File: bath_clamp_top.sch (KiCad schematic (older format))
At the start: 80 parts, among them J1 105-1103-001, J2 105-1103-001, J3 105-1103-001, J4 HDMI_A, K1 1462042-7, K2 1462042-7, Q1 MBT3904DW1T1G, Q3 MBT3904DW1T1G, Q4 MBT3904DW1T1G, U1 OPA828, U12 TCA9555DBR, U13 TCA9555DBR, U19 TMUX6136PWR, U2 ADG1208, U25 OPA2156xD, U3 G6L-1F-TR-DC5, U4 G6L-1F-TR-DC5, U5 G6L-1F-TR-DC5, U8 OPA2156xD

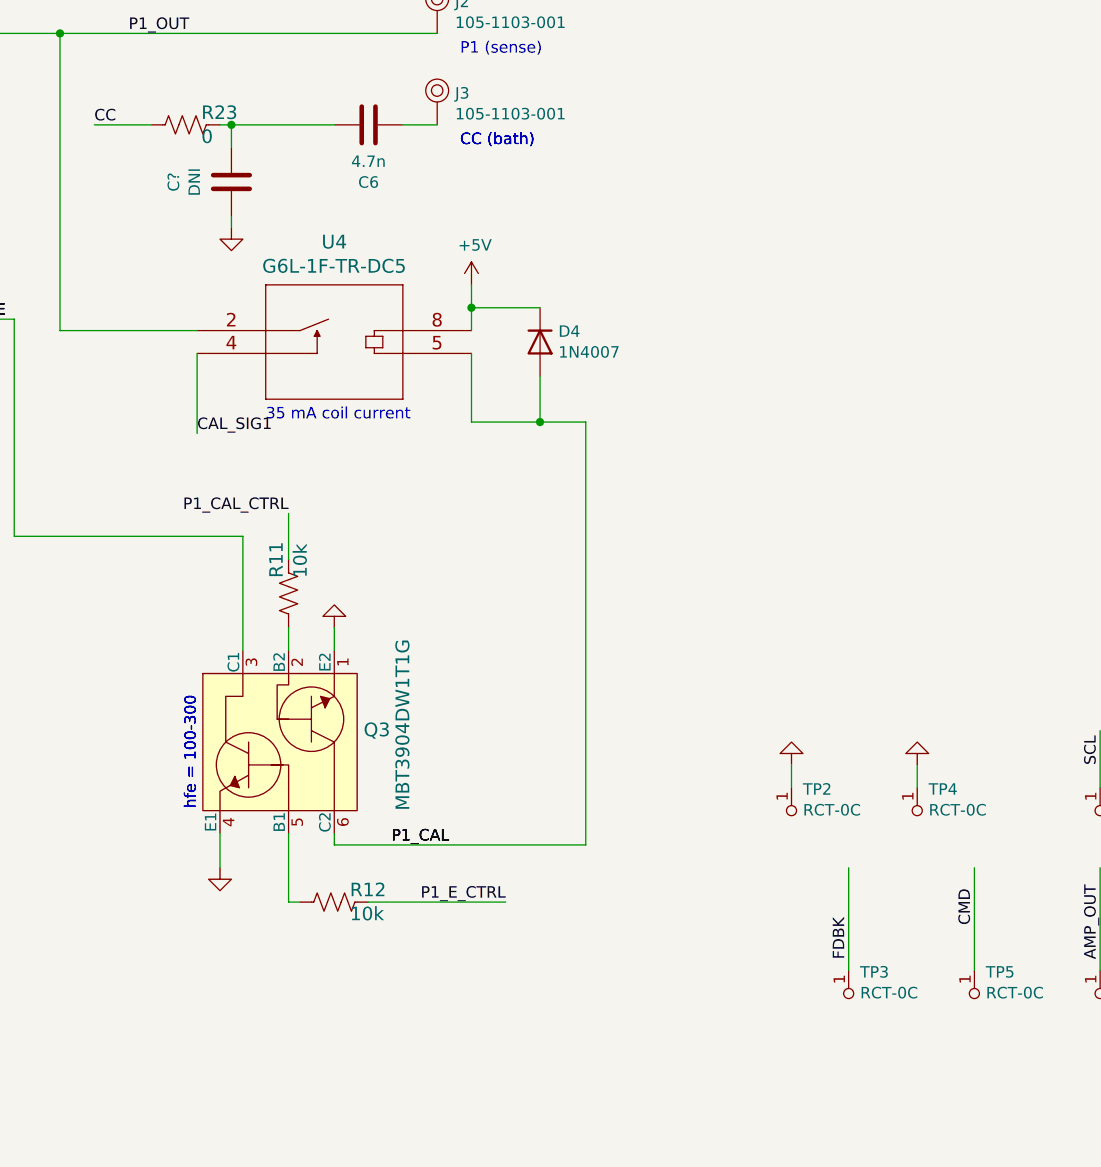
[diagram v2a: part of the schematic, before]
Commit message: nearly completed layout re-route
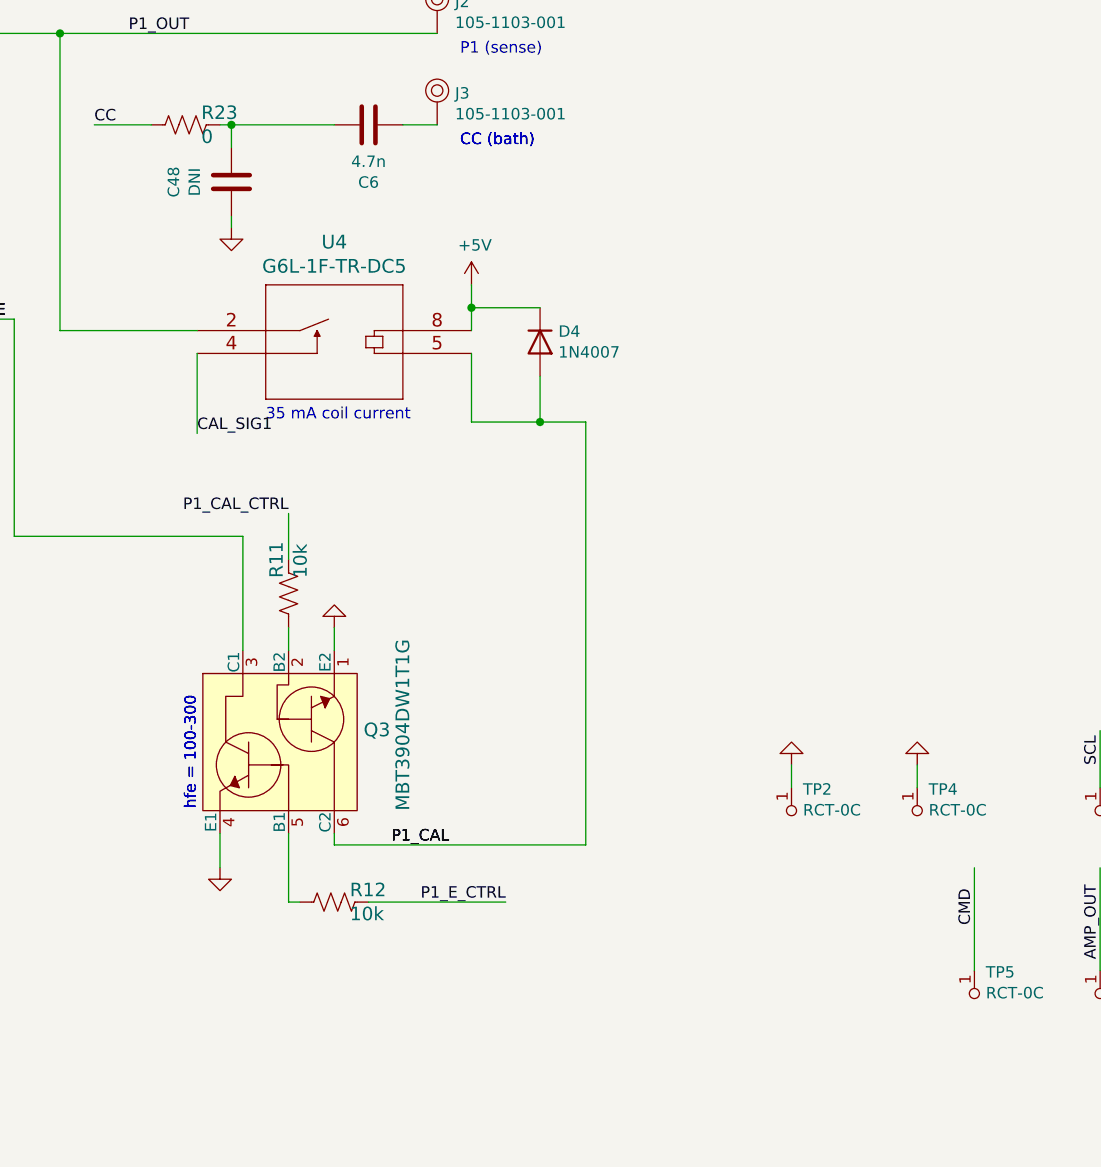
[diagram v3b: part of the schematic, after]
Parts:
- removed TP3: RCT-0C, digikey-footprints:PROBE_PAD_0805, symbol dk_Test-Points:RCT-0C
- gave numbers to parts that had none: 1
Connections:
- wire segments 373 -> 372
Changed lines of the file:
@@
-$EndComp
-$Comp
-L dk_Test-Points:RCT-0C TP3
-U 1 1 6153F62F
-P 14350 9000
-F 0 "TP3" H 14400 9093 50  0000 L CNN
-F 1 "RCT-0C" H 14400 9002 50  0000 L CNN
-F 2 "digikey-footprints:PROBE_PAD_0805" H 14550 9200 60  0001 L CNN
-F 3 "https://www.te.com/commerce/DocumentDelivery/DDEController?Action=srchrtrv&DocNm=1773266&DocType=DS&DocLang=English" H 14550 9300 60  0001 L CNN
-F 4 "A106144CT-ND" H 14550 9400 60  0001 L CNN "Digi-Key_PN"
-F 5 "RCT-0C" H 14550 9500 60  0001 L CNN "MPN"
-F 6 "Test and Measurement" H 14550 9600 60  0001 L CNN "Category"
-F 7 "Test Points" H 14550 9700 60  0001 L CNN "Family"
-F 8 "https://www.te.com/commerce/DocumentDelivery/DDEController?Action=srchrtrv&DocNm=1773266&DocType=DS&DocLang=English" H 14550 9800 60  0001 L CNN "DK_Datasheet_Link"
-F 9 "/product-detail/en/te-connectivity-amp-connectors/RCT-0C/A106144CT-ND/3477801" H 14550 9900 60  0001 L CNN "DK_Detail_Page"
-F 10 "PC TEST POINT NATURAL" H 14550 10000 60  0001 L CNN "Description"
-F 11 "TE Connectivity AMP Connectors" H 14550 10100 60  0001 L CNN "Manufacturer"
-F 12 "Active" H 14550 10200 60  0001 L CNN "Status"
-F 13 "RCT-0C" H 14350 9000 50  0001 C CNN "Manf#"
-	1    14350 9000
-	1    0    0    -1
 $EndComp
 $Comp
@@
 CMD
 Wire Wire Line
-	14350 8900 14350 8450
-Wire Wire Line
 	15450 8100 15450 7850
 Wire Wire Line
@@
 Wire Wire Line
 	14650 8100 14650 8000
-Text Label 14350 8850 1    50   ~ 0
-FDBK
 $Comp
 L dk_Test-Points:RCT-0C TP1
@@
 6.0 mm by \n10.0 mm
 $Comp
-L Device:C C?
+L Device:C C48
 U 1 1 62573817
 P 11650 5450
-F 0 "C?" V 11398 5450 50  0000 C CNN
+F 0 "C48" V 11398 5450 50  0000 C CNN
 F 1 "DNI" V 11489 5450 50  0000 C CNN
 F 2 "Capacitor_SMD:C_0603_1608Metric" H 11688 5300 50  0001 C CNN
@@
 $EndComp
 $Comp
-L power:GND #PWR?
+L power:GND #PWR0188
 U 1 1 625748EF
 P 11650 5650
-F 0 "#PWR?" H 11650 5400 50  0001 C CNN
+F 0 "#PWR0188" H 11650 5400 50  0001 C CNN
 F 1 "GND" V 11655 5522 50  0001 R CNN
 F 2 "" H 11650 5650 50  0001 C CNN
@@
 Wire Wire Line
 	11650 5300 11650 5200
+Connection ~ 11650 5200
+Wire Wire Line
+	11650 5200 12100 5200
 Wire Bus Line
 	9200 9450 9200 9750
@@
 Wire Bus Line
 	3500 8000 3500 8450
-Connection ~ 11650 5200
-Wire Wire Line
-	11650 5200 12100 5200
 $EndSCHEMATC

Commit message: gerbers, BOM and fabrication files sent to PCBway
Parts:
- added C49: DNI, Capacitor_SMD:C_0603_1608Metric, symbol Device:C
- added J5: Conn_01x04, Connector_PinHeader_2.54mm:PinHeader_1x04_P2.54mm_Vertical, symbol Connector_Generic:Conn_01x04
- added TP13, TP14, TP15: TestPoint, TestPoint:TestPoint_THTPad_D2.0mm_Drill1.0mm, symbol Connector:TestPoint
- J1: Category Connectors, Interconnects -> (none); DK_Datasheet_Link https://belfuse.com/resources/Johnson/drawings/dr-105110100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 -> (none); DK_Detail_Page /product-detail/en/cinch-connectivity-solutions-johnson/105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 -> (none); Digi-Key_PN J577-ND -> (none); Family Banana and Tip Connectors - Jacks, Plugs -> (none); MPN 105-1103-001 -> (none); Manufacturer (none) -> Cinch Connectivity Solutions Johnson; Status Active -> (none)
- J2, J3: Category Connectors, Interconnects -> (none); DK_Datasheet_Link https://belfuse.com/resources/Johnson/drawings/dr-105110100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 -> (none); DK_Detail_Page /product-detail/en/cinch-connectivity-solutions-johnson/105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 -> (none); Digi-Key_PN J577-ND -> (none); Family Banana and Tip Connectors - Jacks, Plugs -> (none); MPN 105-1103-001 -> (none); Status Active -> (none)
- K1, K2: footprint covg-kicad:Relay_SPDT_TE_1462042-7 -> RELAY_1462042-8
- Q1: footprint Package_TO_SOT_SMD:SOT-363_SC-70-6 -> digikey-footprints:SOT-363; Category Discrete Semiconductor Products -> (none); DK_Datasheet_Link http://www.onsemi.com/pub/Collateral/MBT3904DW1T1-D.PDF -> (none); DK_Detail_Page /product-detail/en/on-semiconductor/MBT3904DW1T1G/MBT3904DW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 -> (none); Digi-Key_PN MBT3904DW1T1GOSCT-ND -> (none); Family Transistors - Bipolar (BJT) - Arrays -> (none); MPN MBT3904DW1T1G -> (none); Status Active -> (none)
- Q3: footprint Package_TO_SOT_SMD:SOT-363_SC-70-6 -> digikey-footprints:SOT-363; Category Discrete Semiconductor Products -> (none); DK_Datasheet_Link http://www.onsemi.com/pub/Collateral/MBT3904DW1T1-D.PDF -> (none); DK_Detail_Page /product-detail/en/on-semiconductor/MBT3904DW1T1G/MBT3904DW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 -> (none); Digi-Key_PN MBT3904DW1T1GOSCT-ND -> (none); Family Transistors - Bipolar (BJT) - Arrays -> (none); Status Active -> (none)
- Q4: footprint Package_TO_SOT_SMD:SOT-363_SC-70-6 -> digikey-footprints:SOT-363; Category Discrete Semiconductor Products -> (none); DK_Datasheet_Link http://www.onsemi.com/pub/Collateral/MBT3904DW1T1-D.PDF -> (none); DK_Detail_Page /product-detail/en/on-semiconductor/MBT3904DW1T1G/MBT3904DW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 -> (none); Digi-Key_PN MBT3904DW1T1GOSCT-ND -> (none); Family Transistors - Bipolar (BJT) - Arrays -> (none); MPN MBT3904DW1T1G -> (none); Manufacturer (none) -> ON Semiconductor; Status Active -> (none)
- TP4: Category Test and Measurement -> (none); DK_Datasheet_Link https://www.te.com/commerce/DocumentDelivery/DDEController?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 -> (none); Digi-Key_PN A106144CT-ND -> (none); MPN RCT-0C -> (none); Status Active -> (none)
- U19: value TMUX6136PWR -> DNI
- U3: footprint covg-kicad:G6L-1F-TR-DC5 -> G6L-1F-TR-DC5
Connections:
- wire segments 372 -> 383
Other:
- moved on the sheet: C6
